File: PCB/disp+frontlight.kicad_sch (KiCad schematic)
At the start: 19 parts, among them Q1 Si1308EDL

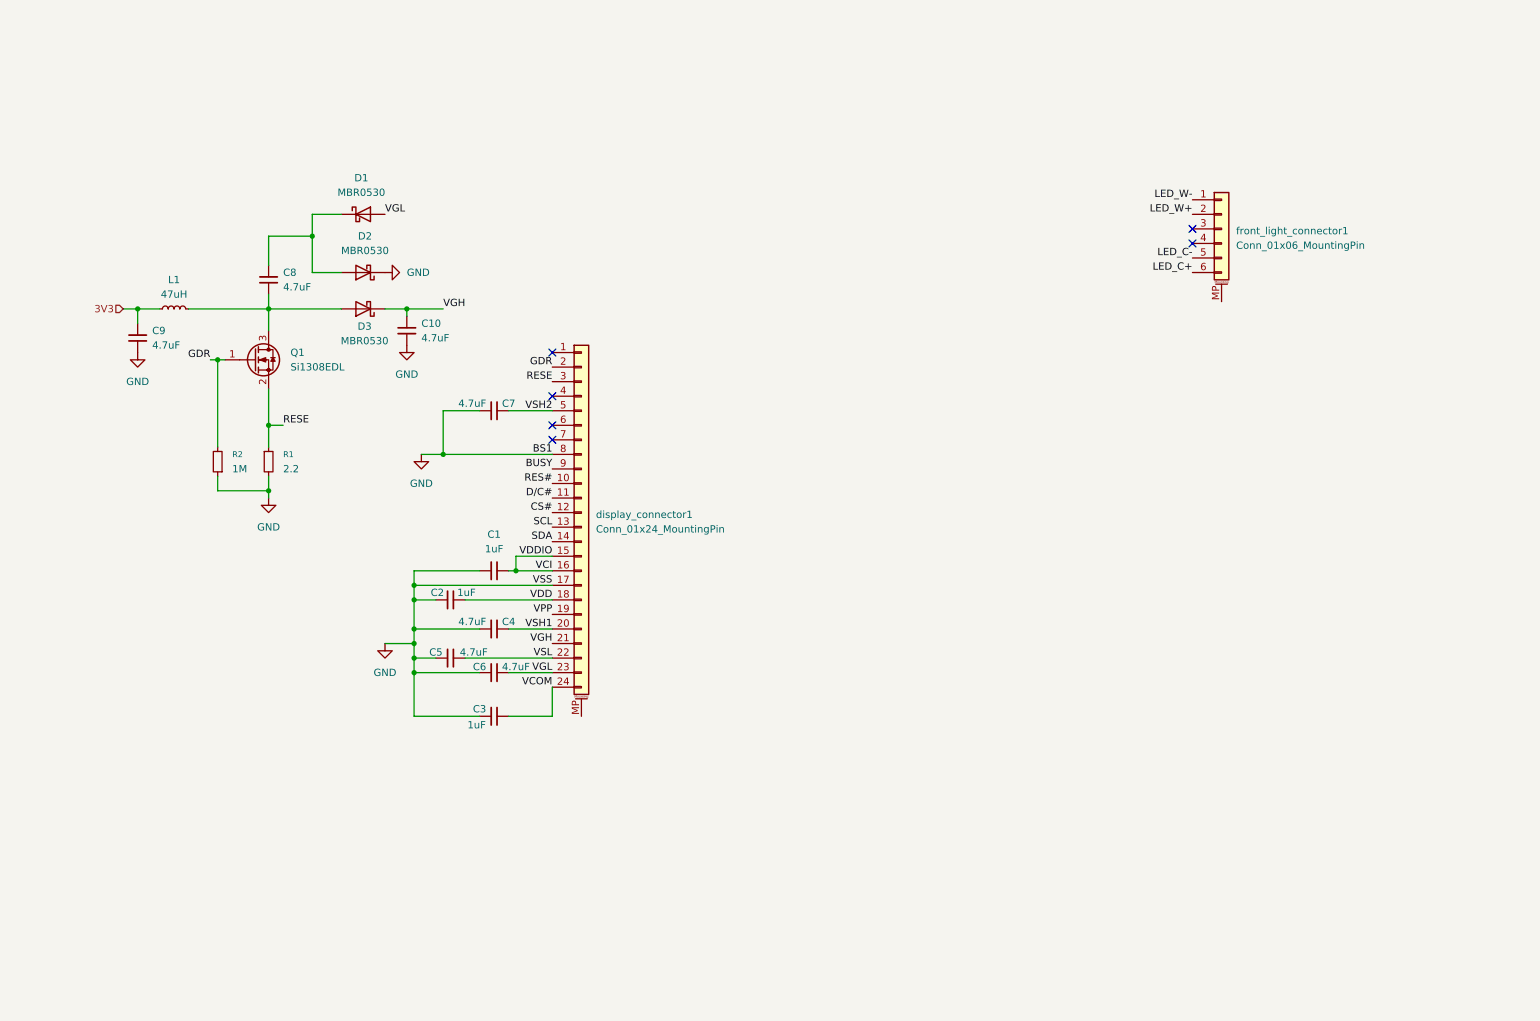
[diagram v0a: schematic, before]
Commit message: Copied over LED from Silkscreen
LED Power control circuit
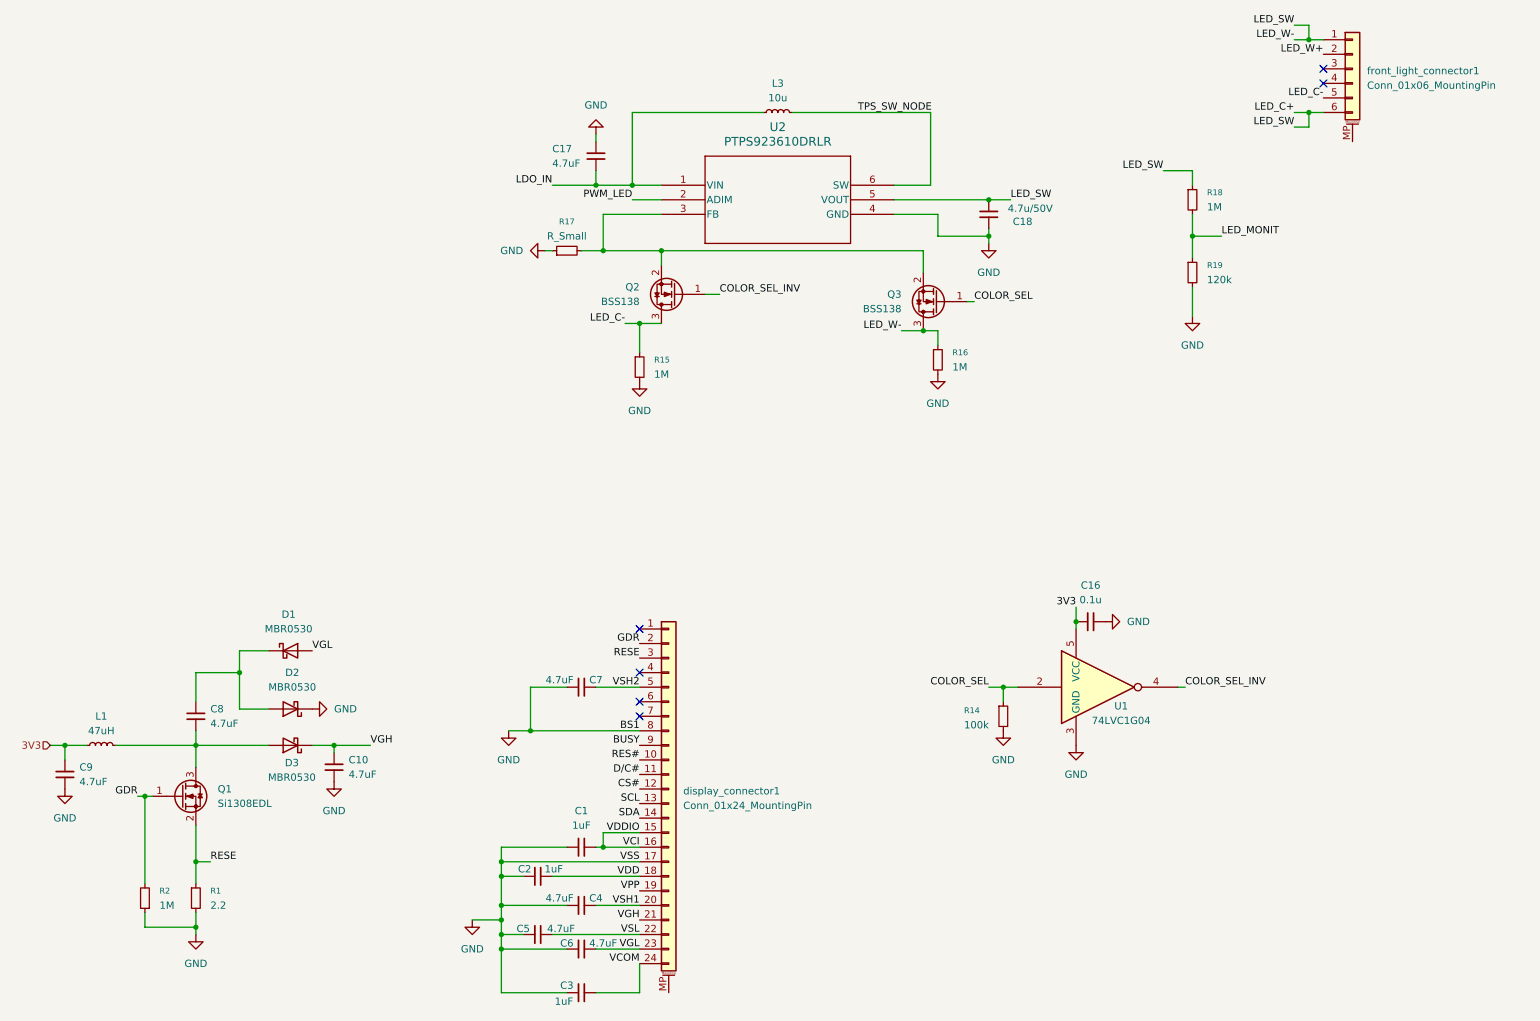
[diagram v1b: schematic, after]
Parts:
- added C16: 0.1u, symbol Device:C_Small
- added C17: 4.7uF, Package_TO_SOT_SMD:SOT-23-6, symbol Device:C_Small
- added C18: 4.7u/50V, Package_TO_SOT_SMD:SOT-23-6, symbol Device:C_Small
- added L3: 10u, Relay_THT:Relay_DPDT_Finder_30.22, symbol Device:L_Small
- added Q2, Q3: BSS138, Package_TO_SOT_SMD:SOT-23, symbol Transistor_FET:BSS138
- added R14: 100k, Package_DIP:DIP-8_W7.62mm, symbol Device:R_Small
- added R15, R18: 1M, Package_DIP:DIP-8_W7.62mm, symbol Device:R_Small
- added R16: 1M, symbol Device:R_Small
- added R17: R_Small, symbol Device:R_Small
- added R19: 120k, Package_DIP:DIP-8_W7.62mm, symbol Device:R_Small
- added U1: 74LVC1G04, symbol 74xGxx:74LVC1G04
- added U2: PTPS923610DRLR, U_DRL0006A_6L_TEX, symbol ul_PTPS923610DRLR:PTPS923610DRLR
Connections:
- net LED_W- is gone; now on net LED_C+: front_light_connector1.1 (Pin_1)
- net 3V3: now also C16.1, U1.5 (VCC)
- net GND: now also C16.2, C17.2, C18.2, R14.2, R15.2, R16.2, R17.1, R19.2, U1.3 (GND), U2.4 (GND)
- net LED_C+: now also C18.1, Q3.3 (D), R16.1, R18.1, U2.5 (VOUT)
- net LED_C-: now also Q2.3 (D), R15.1
- new net: Q2.2 (S), Q3.2 (S), R17.2, U2.3 (FB)
- new net COLOR_SEL: Q3.1 (G), R14.1, U1.2
- new net COLOR_SEL_INV: Q2.1 (G), U1.4
- new net LDO_IN: C17.1, L3.1, U2.1 (VIN)
- new net LED_MONIT: R18.2, R19.1
- new net PWM_LED: U2.2 (ADIM)
- new net TPS_SW_NODE: L3.2, U2.6 (SW)
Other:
- moved on the sheet: C1, C10, C2, C3, C4, C5, C6, C7, C8, C9, D1, D2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

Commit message: Finished schematic
added ldo reg for system power from battery charger ic
finished up all wiring
footprints added
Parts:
- C10, C17, C18, C8, C9: footprint Package_TO_SOT_SMD:SOT-23-6 -> Capacitor_SMD:C_1206_3216Metric_Pad1.33x1.80mm_HandSolder
- C16: footprint (none) -> Capacitor_SMD:C_1206_3216Metric_Pad1.33x1.80mm_HandSolder
- D1, D2, D3: footprint Diode_SMD:D_SOD-123 -> Diode_SMD:D_1206_3216Metric_Pad1.42x1.75mm_HandSolder
- L1: footprint Package_SO:SOIC-20W_7.5x12.8mm_P1.27mm -> Inductor_SMD:L_1206_3216Metric_Pad1.22x1.90mm_HandSolder
- L3: footprint Relay_THT:Relay_DPDT_Finder_30.22 -> Inductor_SMD:L_1206_3216Metric_Pad1.22x1.90mm_HandSolder
- R1: footprint Package_TO_SOT_SMD:SOT-323_SC-70 -> Resistor_SMD:R_1206_3216Metric_Pad1.30x1.75mm_HandSolder
- R14, R15, R18, R19: footprint Package_DIP:DIP-8_W7.62mm -> Resistor_SMD:R_1206_3216Metric_Pad1.30x1.75mm_HandSolder
- R16, R17, R2: footprint (none) -> Resistor_SMD:R_1206_3216Metric_Pad1.30x1.75mm_HandSolder
- U1: footprint (none) -> Package_TO_SOT_SMD:SOT-323_SC-70
- U2: footprint U_DRL0006A_6L_TEX -> Package_TO_SOT_SMD:TSOT-23
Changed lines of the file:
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@@
 			)
 		)
-		(property "Footprint" "Package_TO_SOT_SMD:SOT-23-6"
+		(property "Footprint" "Capacitor_SMD:C_1206_3216Metric_Pad1.33x1.80mm_HandSolder"
 			(at 49.53 138.43 0)
 			(hide yes)
@@
 			)
 		)
-		(property "Footprint" "Package_DIP:DIP-8_W7.62mm"
+		(property "Footprint" "Resistor_SMD:R_1206_3216Metric_Pad1.30x1.75mm_HandSolder"
 			(at 223.52 60.96 0)
 			(hide yes)
@@
 			)
 		)
-		(property "Footprint" "Package_TO_SOT_SMD:SOT-23-6"
+		(property "Footprint" "Capacitor_SMD:C_1206_3216Metric_Pad1.33x1.80mm_HandSolder"
 			(at 73.66 147.32 0)
 			(hide yes)
@@
 			)
 		)
-		(property "Footprint" "Package_TO_SOT_SMD:SOT-23-6"
+		(property "Footprint" "Capacitor_SMD:C_1206_3216Metric_Pad1.33x1.80mm_HandSolder"
 			(at 26.67 148.59 0)
 			(hide yes)
@@
 			)
 		)
-		(property "Footprint" "Package_SO:SOIC-20W_7.5x12.8mm_P1.27mm"
+		(property "Footprint" "Inductor_SMD:L_1206_3216Metric_Pad1.22x1.90mm_HandSolder"
 			(at 33.02 143.51 0)
 			(hide yes)
@@
 			)
 		)
-		(property "Footprint" "Relay_THT:Relay_DPDT_Finder_30.22"
+		(property "Footprint" "Inductor_SMD:L_1206_3216Metric_Pad1.22x1.90mm_HandSolder"
 			(at 151.13 33.02 0)
 			(hide yes)
@@
 			)
 		)
-		(property "Footprint" "U_DRL0006A_6L_TEX"
+		(property "Footprint" "Package_TO_SOT_SMD:TSOT-23"
 			(at 130.81 45.72 0)
 			(hide yes)
@@
 			)
 		)
-		(property "Footprint" "Diode_SMD:D_SOD-123"
+		(property "Footprint" "Diode_SMD:D_1206_3216Metric_Pad1.42x1.75mm_HandSolder"
 			(at 66.04 139.065 0)
 			(hide yes)
@@
 			)
 		)
-		(property "Footprint" ""
+		(property "Footprint" "Package_TO_SOT_SMD:SOT-323_SC-70"
 			(at 208.28 133.35 0)
 			(hide yes)
@@
 			)
 		)
-		(property "Footprint" "Package_TO_SOT_SMD:SOT-23-6"
+		(property "Footprint" "Capacitor_SMD:C_1206_3216Metric_Pad1.33x1.80mm_HandSolder"
 			(at 119.38 40.64 0)
 			(hide yes)
@@
 			)
 		)
-		(property "Footprint" "Package_DIP:DIP-8_W7.62mm"
+		(property "Footprint" "Resistor_SMD:R_1206_3216Metric_Pad1.30x1.75mm_HandSolder"
 			(at 127 77.47 0)
 			(hide yes)
@@
 			)
 		)
-		(property "Footprint" "Package_DIP:DIP-8_W7.62mm"
+		(property "Footprint" "Resistor_SMD:R_1206_3216Metric_Pad1.30x1.75mm_HandSolder"
 			(at 223.52 48.26 0)
 			(hide yes)
@@
 			)
 		)
-		(property "Footprint" ""
+		(property "Footprint" "Capacitor_SMD:C_1206_3216Metric_Pad1.33x1.80mm_HandSolder"
 			(at 205.74 121.92 0)
 			(hide yes)
@@
 			)
 		)
-		(property "Footprint" "Package_DIP:DIP-8_W7.62mm"
+		(property "Footprint" "Resistor_SMD:R_1206_3216Metric_Pad1.30x1.75mm_HandSolder"
 			(at 190.5 138.43 0)
 			(hide yes)
@@
 			)
 		)
-		(property "Footprint" "Package_TO_SOT_SMD:SOT-323_SC-70"
+		(property "Footprint" "Resistor_SMD:R_1206_3216Metric_Pad1.30x1.75mm_HandSolder"
 			(at 49.53 170.18 0)
 			(hide yes)
@@
 			)
 		)
-		(property "Footprint" ""
+		(property "Footprint" "Resistor_SMD:R_1206_3216Metric_Pad1.30x1.75mm_HandSolder"
 			(at 179.07 76.2 0)
 			(hide yes)
@@
 			)
 		)
-		(property "Footprint" ""
+		(property "Footprint" "Resistor_SMD:R_1206_3216Metric_Pad1.30x1.75mm_HandSolder"
 			(at 114.3 57.15 0)
 			(hide yes)
@@
 			)
 		)
-		(property "Footprint" ""
+		(property "Footprint" "Resistor_SMD:R_1206_3216Metric_Pad1.30x1.75mm_HandSolder"
 			(at 40.64 170.18 0)
 			(hide yes)
@@
 			)
 		)
-		(property "Footprint" "Diode_SMD:D_SOD-123"
+		(property "Footprint" "Diode_SMD:D_1206_3216Metric_Pad1.42x1.75mm_HandSolder"
 			(at 66.04 132.715 0)
 			(hide yes)
@@
 			)
 		)
-		(property "Footprint" "Diode_SMD:D_SOD-123"
+		(property "Footprint" "Diode_SMD:D_1206_3216Metric_Pad1.42x1.75mm_HandSolder"
 			(at 66.04 131.445 0)
 			(hide yes)
@@
 			)
 		)
-		(property "Footprint" "Package_TO_SOT_SMD:SOT-23-6"
+		(property "Footprint" "Capacitor_SMD:C_1206_3216Metric_Pad1.33x1.80mm_HandSolder"
 			(at 187.96 50.8 0)
 			(hide yes)

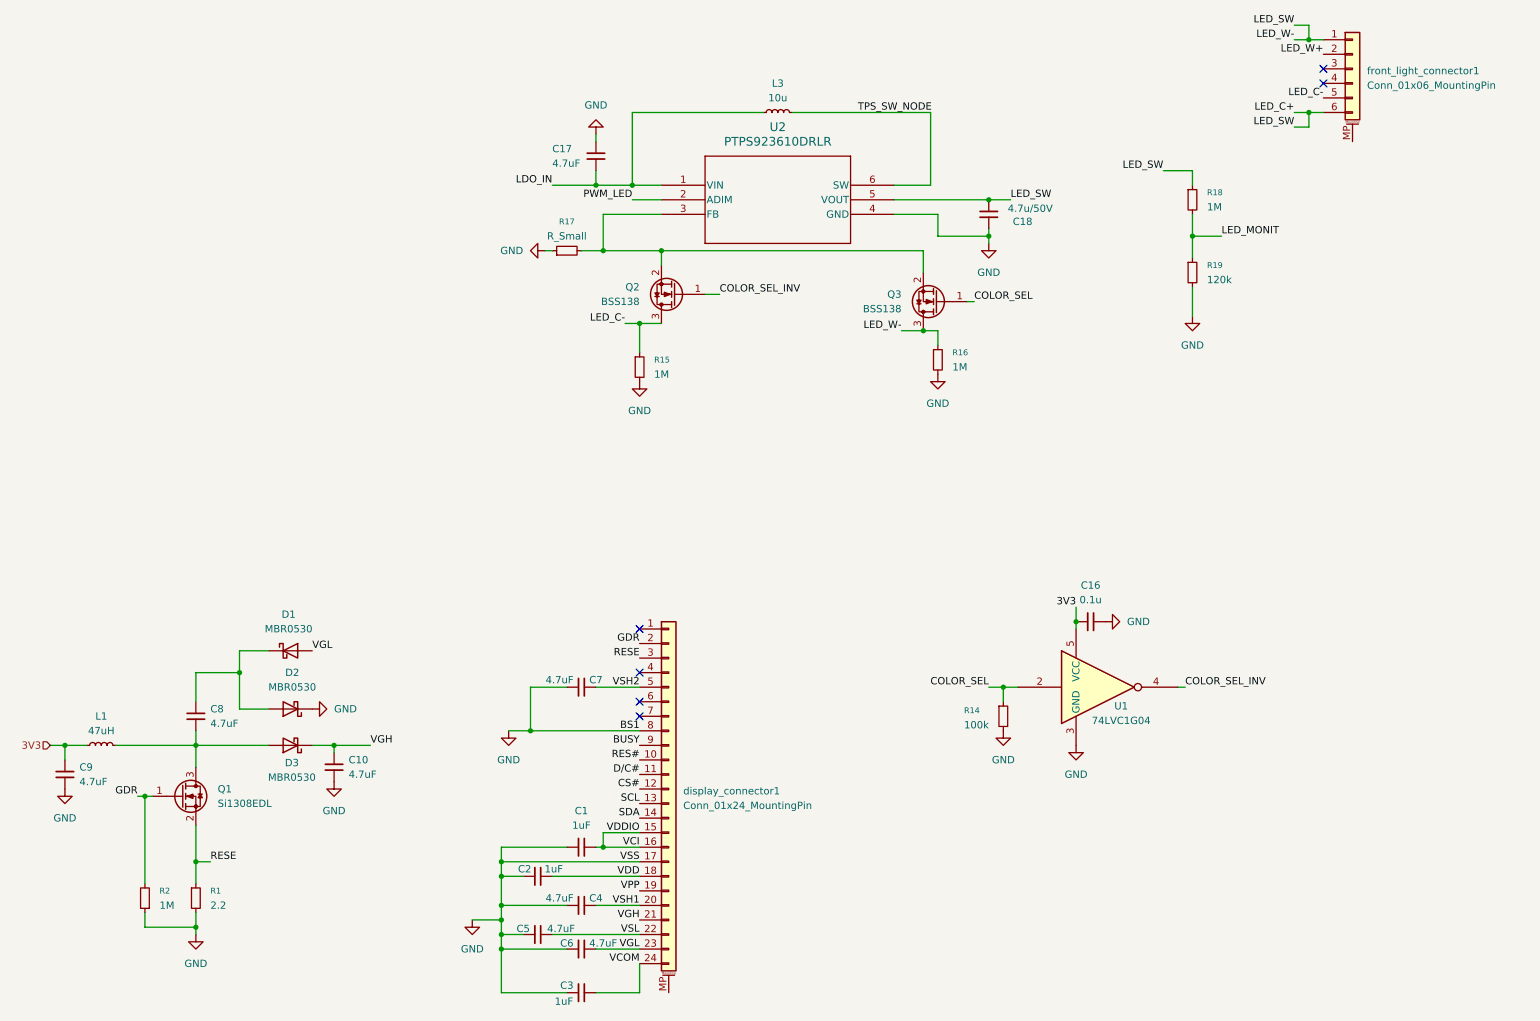
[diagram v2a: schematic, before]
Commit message: PCB and BOM
Pulled stuff onto the PCB and regenerated the BOM to go into ours. Found some components (mostly caps and resistors) that are missing values so will need to update those.
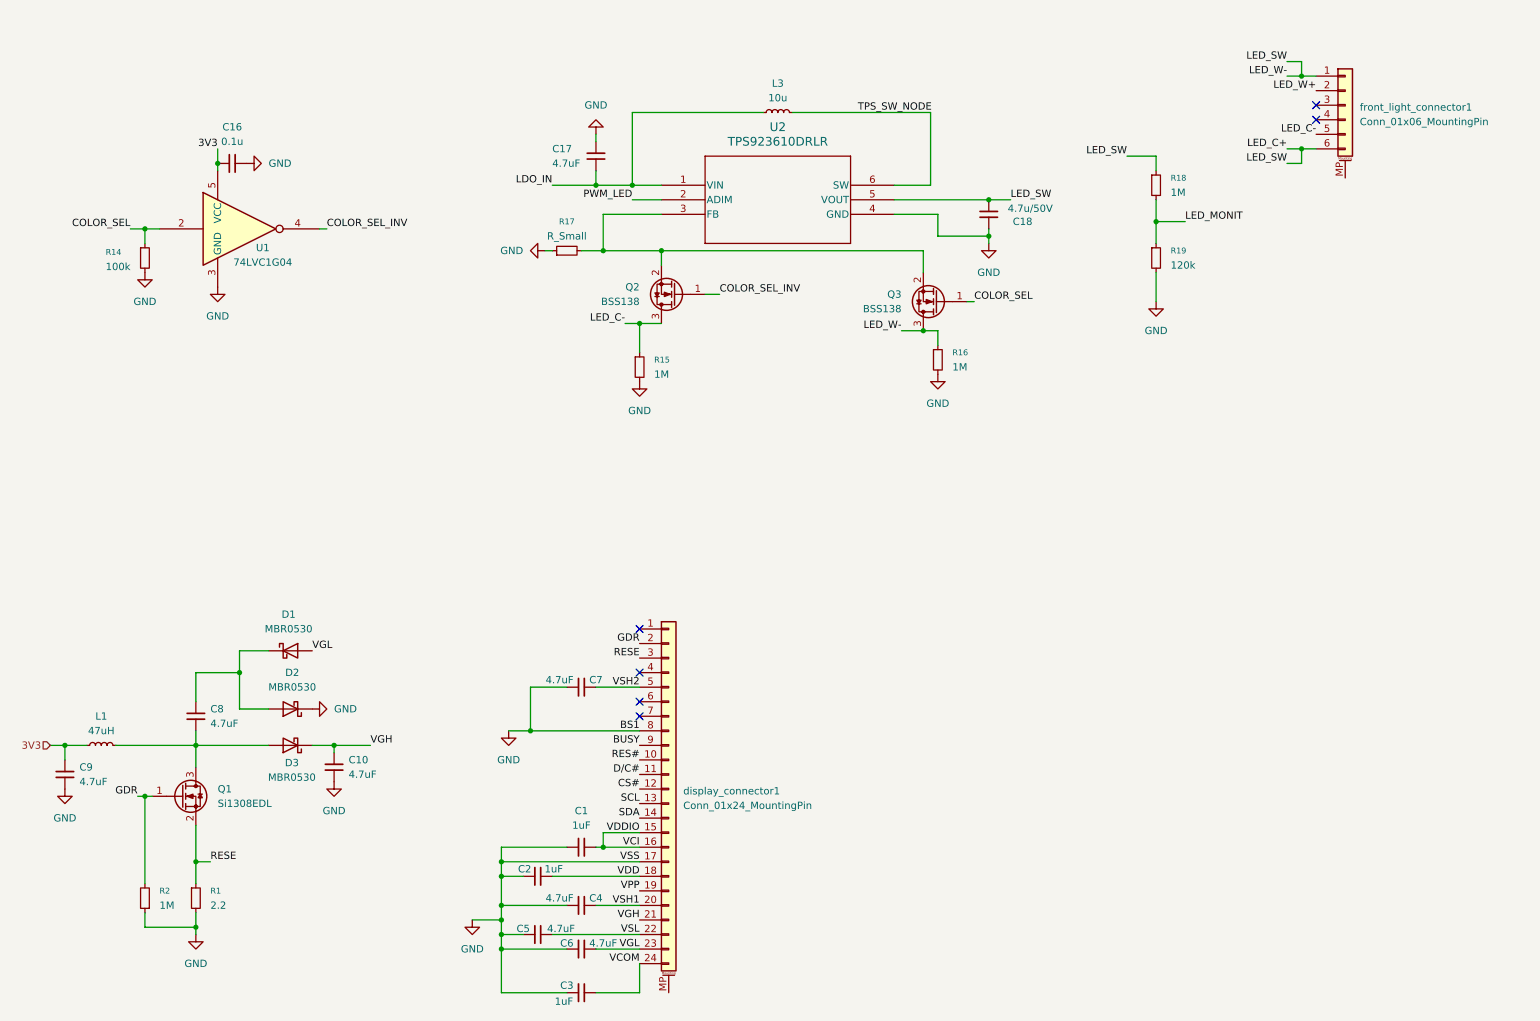
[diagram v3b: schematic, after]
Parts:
- U2: value PTPS923610DRLR -> TPS923610DRLR
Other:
- moved on the sheet: C16, R14, R18, R19, U1, front_light_connector1

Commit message: Rechecked schematic + started PCB
Schematic:
+ routed screen connector
+ fixed charger to 500mA and routed data to MCU
+ added micro sd card reader
+ added uart, jtag, and boot selector pins
= changed esp32 symbol
= made 3v3 a power symbol (idk why i didnt do this from the start)

TODO:
pick resistor values for thermistor
put all passives on pcb
route pcb
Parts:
- Q1: footprint Package_TO_SOT_SMD:SOT-323_SC-70 -> Package_TO_SOT_SMD:SOT-23_Handsoldering
- Q2, Q3: footprint Package_TO_SOT_SMD:SOT-23 -> Package_TO_SOT_SMD:SOT-23_Handsoldering
- U1: footprint Package_TO_SOT_SMD:SOT-323_SC-70 -> Package_TO_SOT_SMD:SOT-23-5_HandSoldering
- U2: footprint Package_TO_SOT_SMD:TSOT-23 -> Package_TO_SOT_SMD:SOT-563
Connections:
- net 3V3 renamed +3V3
- net VPP: no longer names the net of display_connector1.19 (Pin_19)
- no-connect marks 6 -> 9
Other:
- moved on the sheet: C16
